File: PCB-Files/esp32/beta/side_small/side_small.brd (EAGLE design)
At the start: 20 x 17 mm, 11 parts

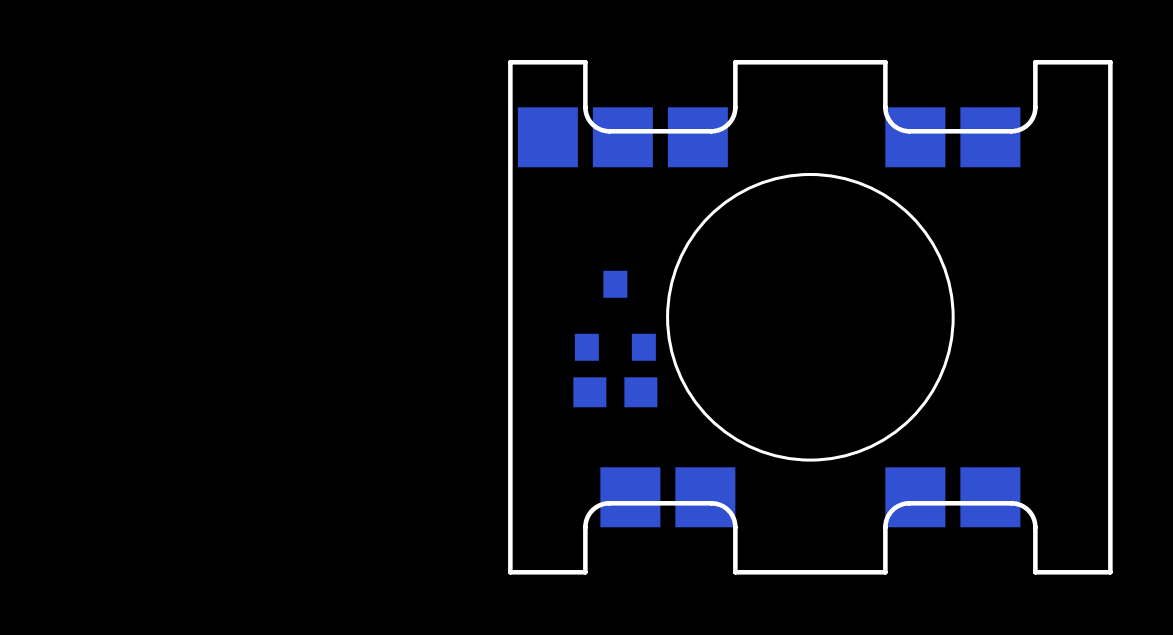
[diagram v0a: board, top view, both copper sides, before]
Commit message: creates final PCB version; revised beta side pcbs to match beta main pcb pinouts
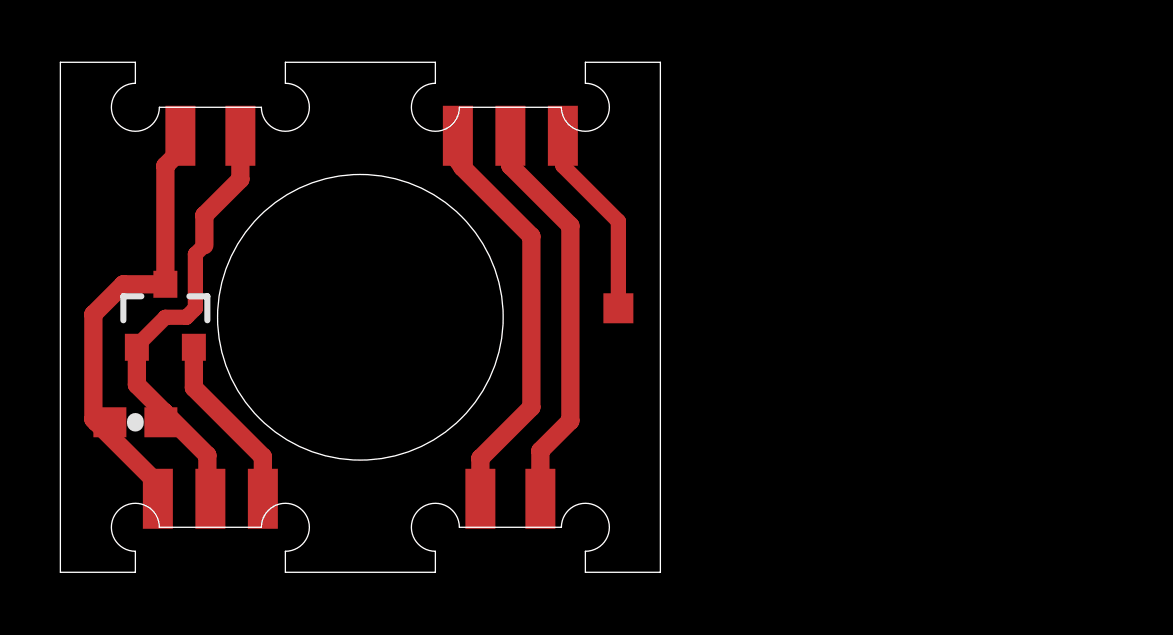
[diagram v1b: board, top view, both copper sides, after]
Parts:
- removed HALL_1_IN, HALL_1_OUT, HALL_1_OUT1, HALL_2_IN, HALL_2_IN1, HALL_GND, HALL_GND1, HALL_VCC, HALL_VCC1: TPTP20SQ, testpad:TP20SQ
- added TP1, TP10, TP11, TP12, TP13, TP14, TP15, TP16, TP17, TP18, TP19, TP2, TP20, TP23, TP3, TP4, TP5, TP6, TP7, TP8, TP9: TPTP10SQ, testpad:TP10SQ
- moved C3 16.0 mm to (2.50, 5.00), flipped to the top, turned to 0 degrees
- moved HALL 15.0 mm to (3.50, 8.50), flipped to the top
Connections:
- new net TOUCH: TP19.TP, TP20.TP, TP23.TP
- net GND: now also TP10.TP, TP15.TP, TP18.TP, TP5.TP; no longer HALL_GND.TP, HALL_GND1.TP
- net HALL_1: now also TP12.TP, TP16.TP, TP2.TP, TP7.TP; no longer HALL_1_IN.TP, HALL_1_OUT.TP
- net HALL_2: now also TP13.TP, TP17.TP, TP3.TP, TP8.TP; no longer HALL_1_OUT1.TP, HALL_2_IN.TP
- net HALL_3: now also TP4.TP, TP9.TP; no longer HALL_2_IN1.TP
- net VCC: now also TP1.TP, TP11.TP, TP14.TP, TP6.TP; no longer HALL_VCC.TP, HALL_VCC1.TP
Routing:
- net GND: track 0.00 -> 16.5 mm
- net VCC: track 0.00 -> 16.3 mm
- net HALL_2: track 0.00 -> 14.8 mm
- net HALL_1: track 0.00 -> 14.3 mm
- net TOUCH: track 0.00 -> 7.30 mm
- net HALL_3: track 0.00 -> 6.50 mm
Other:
- outline, holes or cut-outs redrawn
